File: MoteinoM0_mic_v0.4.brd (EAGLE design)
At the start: 76.5 x 22.9 mm, 39 parts, among them J1 BNCPTH, J3 GND, J9 MIC_OUT, U1 SPU0410LR5H-QB, U2 OPA1679IRUMT, U3 OPA1677DBVX, U4 APFA3010SEKJ3ZGKQBKC

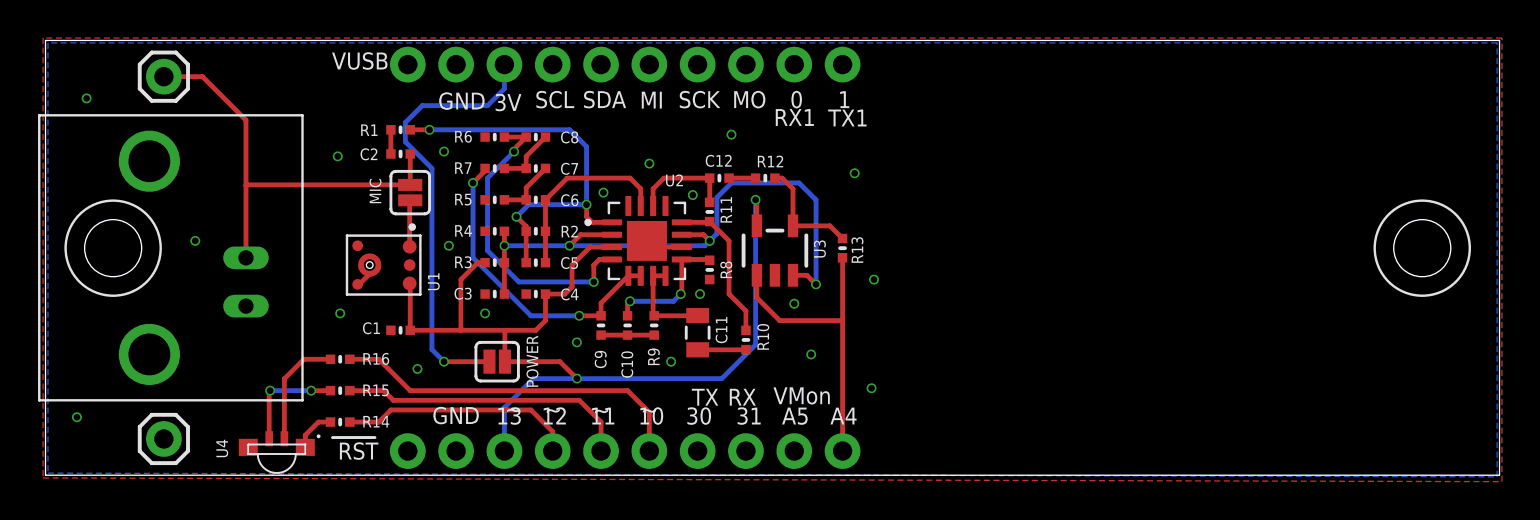
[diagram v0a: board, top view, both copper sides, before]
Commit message: v0.4
- removed stage 5
- board size update
- header size increased
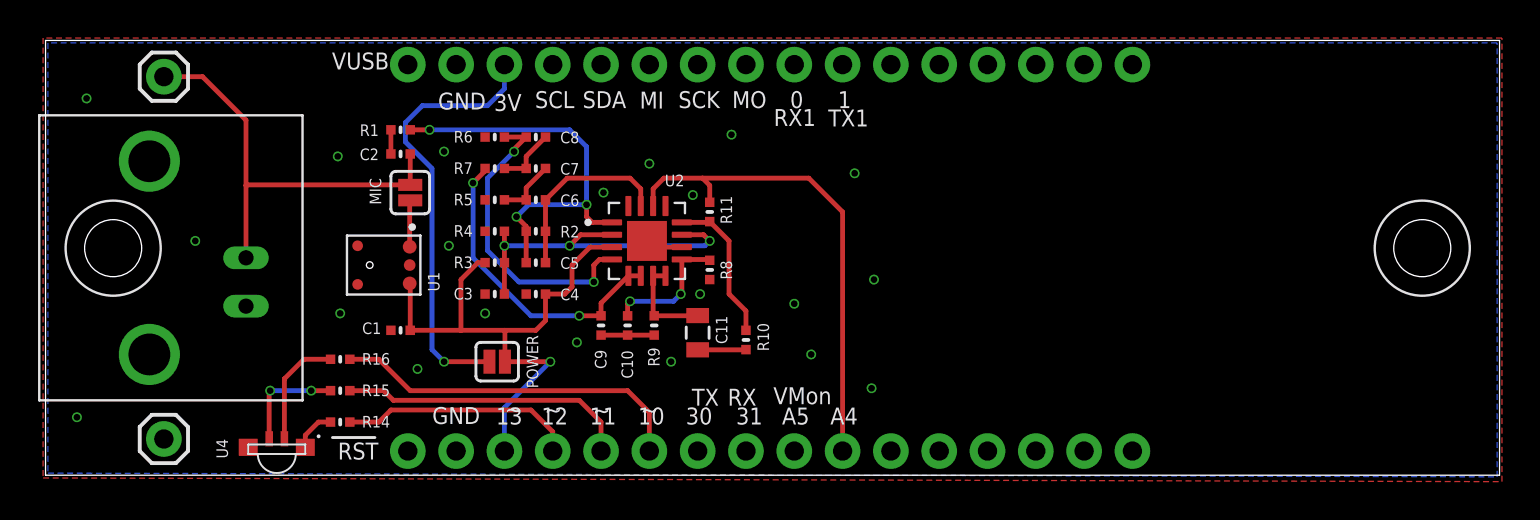
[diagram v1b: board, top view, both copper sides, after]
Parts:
- removed C12: 10nF, Adafruit Feather 32u4 Bluefruit LE:MICROBUILDER__0402MP
- removed J5, J6: (no value), SparkFun-Connectors:1X10_NO_SILK
- removed R12: 1K, Adafruit Feather 32u4 Bluefruit LE:MICROBUILDER__0402MP
- removed R13: 10K, Adafruit Feather 32u4 Bluefruit LE:MICROBUILDER__0402MP
- removed U3: OPA1677DBVX, OPA1677DBV:SOT23-5
- added J2, J4: (no value), SparkFun-Connectors:1X16_NO_SILK
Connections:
- removed net N$17: C12.2, R12.2
- removed net N$18: R12.1, R13.1, U3.4
- removed net STAGE4_OUT: C12.1, R11.2, U2.14
- net !RESET: now also J4.1; no longer J6.1
- net 3.3V: now also J2.3; no longer J5.3
- net A5: now also J4.9; no longer J6.9
- net BLUE: now also J4.6; no longer J6.6
- net D0/RXI: now also J2.9; no longer J5.9
- net D1/TXI: now also J2.10; no longer J5.10
- net GND: now also J2.2, J4.2; no longer J5.2, J6.2, U1.6, U3.2
- net GREEN: now also J4.5; no longer J6.5
- net IN1+: no longer U3.3
- net OUT: now also J4.10, R11.2, U2.14; no longer J6.10, R13.2, U3.1
- net PB22/TXD: now also J4.7; no longer J6.7
- net PB23/RXD: now also J4.8; no longer J6.8
- net POWER: now also J4.3; no longer J6.3, U3.5
- net RED: now also J4.4; no longer J6.4
- net SCL: now also J2.4; no longer J5.4
- net SDA: now also J2.5; no longer J5.5
- net SPI_MISO: now also J2.6; no longer J5.6
- net SPI_MOSI: now also J2.8; no longer J5.8
- net SPI_SCK: now also J2.7; no longer J5.7
- net VUSB: now also J2.1; no longer J5.1
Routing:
- net POWER: track 52.4 -> 30.4 mm, vias 2 -> 1
- net IN1+: track 32.5 -> 18.3 mm, vias 4 -> 3
- net OUT: track 16.3 -> 25.8 mm
- net N$18: track 6.01 -> 0.00 mm
- net STAGE4_OUT: track 5.38 -> 0.00 mm
- net N$17: track 1.40 -> 0.00 mm
- net GND: track 2.82 -> 1.97 mm
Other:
- board text added: "Moteino M0 Mic Board v0.4 | 2022-04-08"
- board text removed: "Moteino M0 Mic Board v0.3 | 2022-03-16"
